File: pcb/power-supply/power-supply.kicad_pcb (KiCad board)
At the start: 2 copper layers, 2 parts

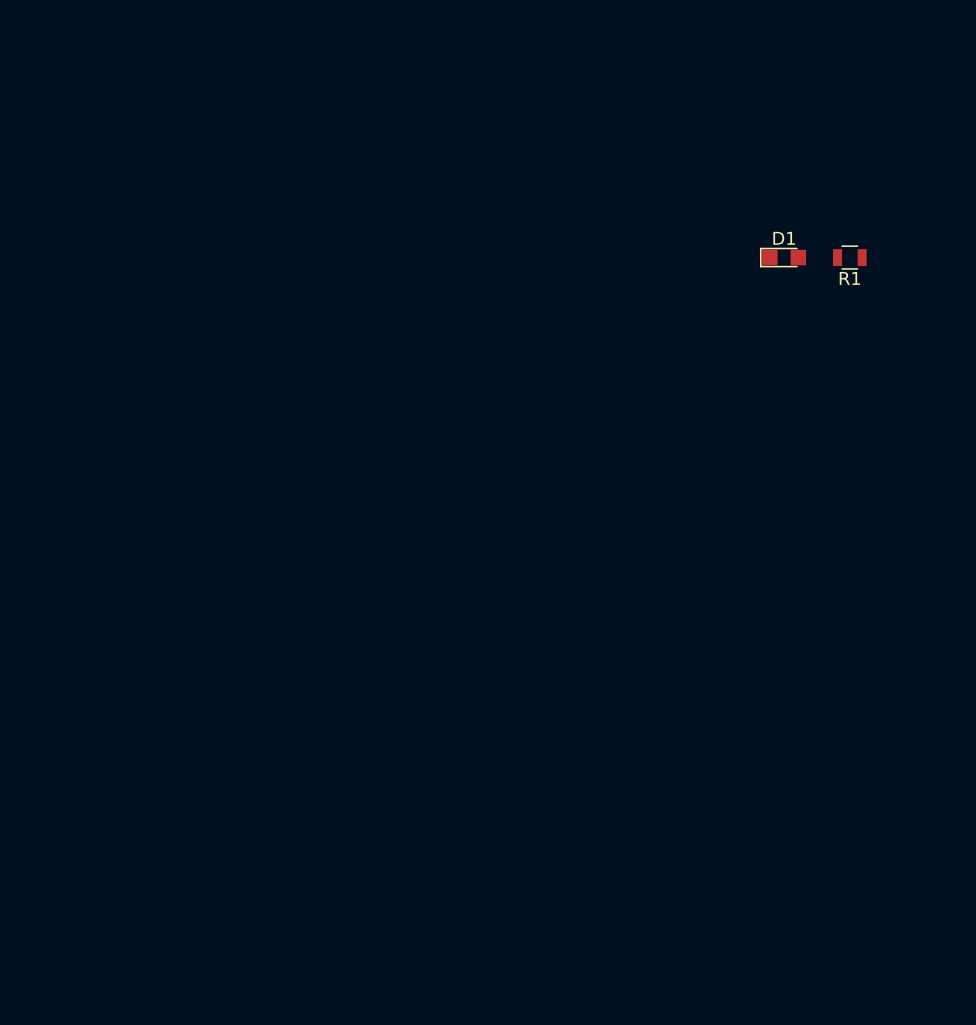
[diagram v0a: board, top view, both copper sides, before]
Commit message: starting the pcb circuit design and the layout design. implementing a RJ45 plug, spi pin-header, adc inputs etc
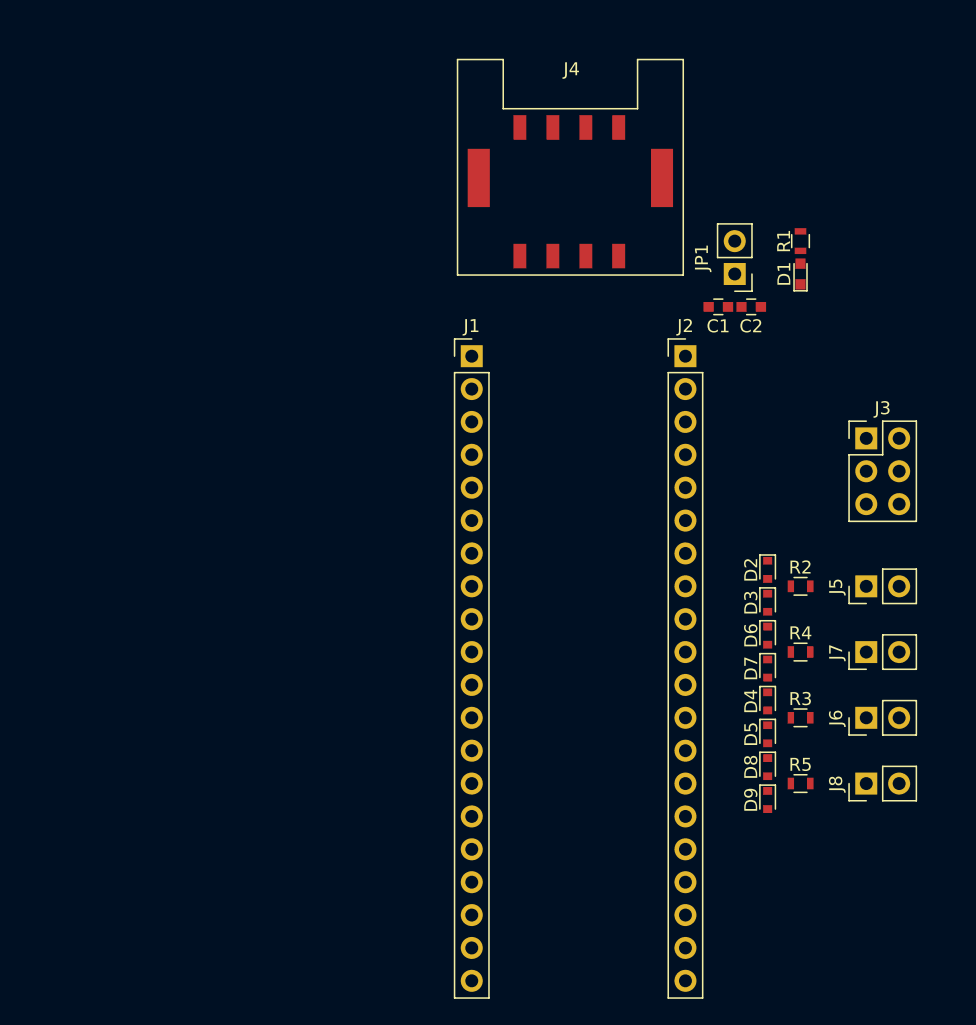
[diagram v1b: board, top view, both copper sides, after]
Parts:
- added C1: 100n, Capacitors_SMD:C_0603, F.Cu at (135.9, 113.0)
- added C2: 100n, Capacitors_SMD:C_0603, F.Cu at (138.4, 113.0)
- added D2: D, Diodes_SMD:D_SOD-523, F.Cu at (139.7, 133.3)
- added D3: D, Diodes_SMD:D_SOD-523, F.Cu at (139.7, 135.9)
- added D4: D, Diodes_SMD:D_SOD-523, F.Cu at (139.7, 143.5)
- added D5: D, Diodes_SMD:D_SOD-523, F.Cu at (139.7, 146.1)
- added D6: D, Diodes_SMD:D_SOD-523, F.Cu at (139.7, 138.4)
- added D7: D, Diodes_SMD:D_SOD-523, F.Cu at (139.7, 141.0)
- added D8: D, Diodes_SMD:D_SOD-523, F.Cu at (139.7, 148.6)
- added D9: D, Diodes_SMD:D_SOD-523, F.Cu at (139.7, 151.1)
- added J1: Conn_01x20_Female, Socket_Strips:Socket_Strip_Straight_1x20_Pitch2.54mm, F.Cu at (116.8, 116.8)
- added J2: Conn_01x20_Female, Socket_Strips:Socket_Strip_Straight_1x20_Pitch2.54mm, F.Cu at (133.3, 116.8)
- added J3: Conn_02x03, Pin_Headers:Pin_Header_Straight_2x03_Pitch2.54mm, F.Cu at (147.3, 123.2)
- added J4: RJ45, Connectors:IQRF_KON-SIM-01, F.Cu at (124.5, 104.1)
- added J5: Conn_01x02, Pin_Headers:Pin_Header_Straight_1x02_Pitch2.54mm, F.Cu at (147.3, 134.6)
- added J6: Conn_01x02, Pin_Headers:Pin_Header_Straight_1x02_Pitch2.54mm, F.Cu at (147.3, 144.8)
- added J7: Conn_01x02, Pin_Headers:Pin_Header_Straight_1x02_Pitch2.54mm, F.Cu at (147.3, 139.7)
- added J8: Conn_01x02, Pin_Headers:Pin_Header_Straight_1x02_Pitch2.54mm, F.Cu at (147.3, 149.9)
- added JP1: JP, Pin_Headers:Pin_Header_Straight_1x02_Pitch2.54mm, F.Cu at (137.2, 110.5)
- added R2: 100k, Resistors_SMD:R_0603, F.Cu at (142.2, 134.6)
- added R3: 100k, Resistors_SMD:R_0603, F.Cu at (142.2, 144.8)
- added R4: 100k, Resistors_SMD:R_0603, F.Cu at (142.2, 139.7)
- added R5: 100k, Resistors_SMD:R_0603, F.Cu at (142.2, 149.9)
- D1: footprint LEDs:LED_0805 -> LEDs:LED_0603
- R1: value R -> 150; footprint Resistors_SMD:R_0805 -> Resistors_SMD:R_0603
- moved R1 4.02 mm to (142.2, 108.0), turned to 270 degrees
- moved D1 1.80 mm to (142.2, 110.5), turned to 90 degrees
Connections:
- R1 pad 1: VCC -> +5V

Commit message: removed RJ45 (should have been a RJ11) with a simple 03x01 pinheader for uart
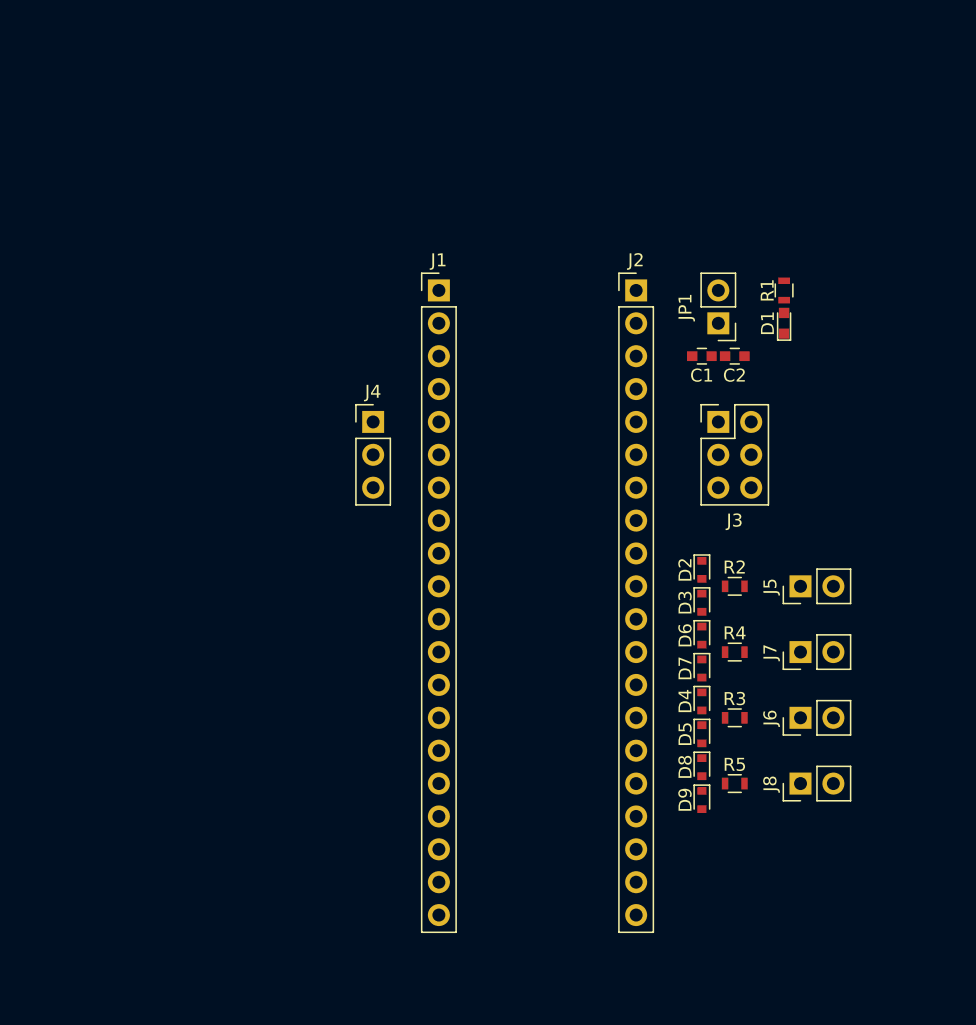
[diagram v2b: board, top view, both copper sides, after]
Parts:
- J4: value RJ45 -> Conn_01x03; footprint Connectors:IQRF_KON-SIM-01 -> Pin_Headers:Pin_Header_Straight_1x03_Pitch2.54mm
- moved J4 23.4 mm to (109.2, 121.9)
- moved J3 11.5 mm to (135.9, 121.9)
- moved J2 6.35 mm to (129.5, 111.8)
- moved J1 5.68 mm to (114.3, 111.8)
- moved R2 5.08 mm to (137.2, 134.6)
- moved R3 5.08 mm to (137.2, 144.8)
- moved R4 5.08 mm to (137.2, 139.7)
- moved R5 5.08 mm to (137.2, 149.9)
- moved D2 5.08 mm to (134.6, 133.3)
- moved D3 5.08 mm to (134.6, 135.9)
- moved D4 5.08 mm to (134.6, 143.5)
- moved D5 5.08 mm to (134.6, 146.1)
- moved D6 5.08 mm to (134.6, 138.4)
- moved D7 5.08 mm to (134.6, 141.0)
- moved D8 5.08 mm to (134.6, 148.6)
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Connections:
- J4 pad 1: Net-(J4-Pad1) -> /D2
- J4 pad 2: /D2 -> /D3
- J4 pad 3: /D3 -> GND

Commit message: added the teensy schematic and footprint lib to the project, added the project from mr veigl to git, added teensy++2.0 to the schematic, added molex connectors, 02x05 pinheaders for motor control signals
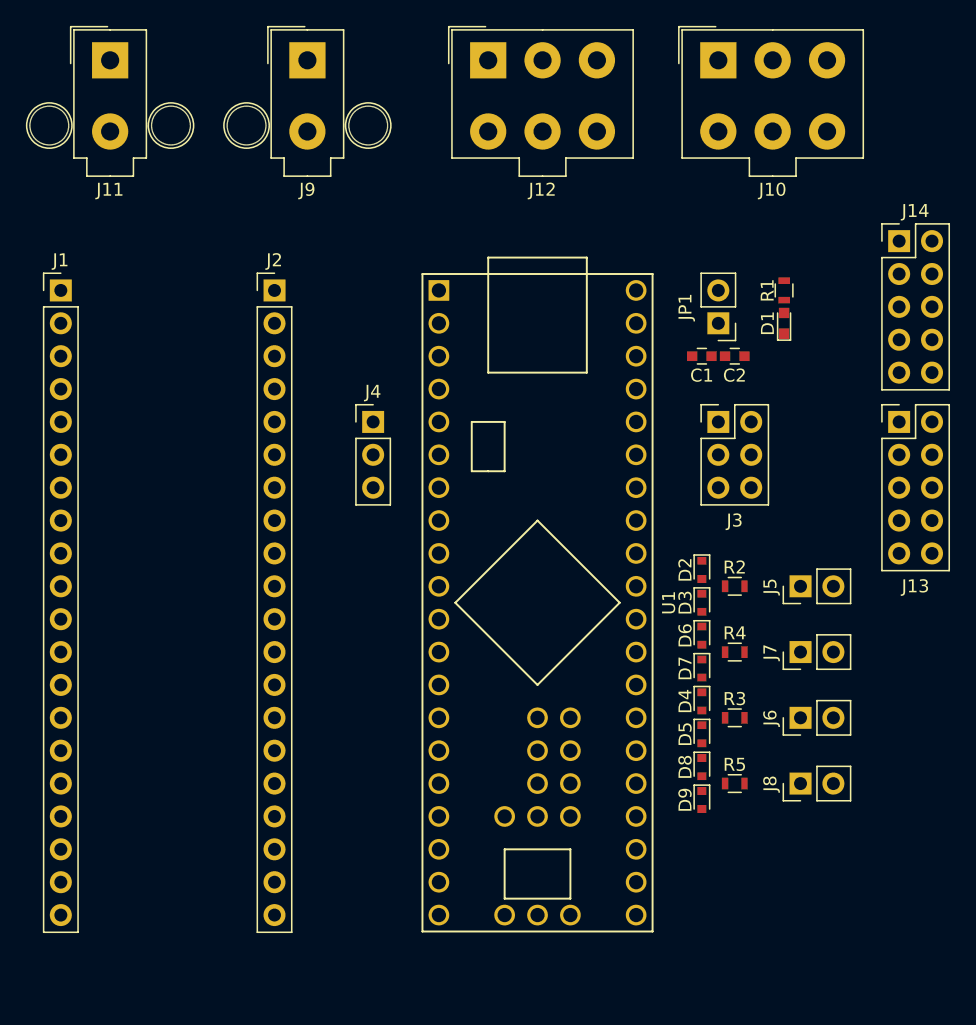
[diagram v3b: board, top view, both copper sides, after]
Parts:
- added J10: Pwr_Terminal, Connectors_Molex:Molex_MiniFit-JR-5556-06A_2x03x4.20mm_Straight, F.Cu at (135.9, 94.0)
- added J11: Pwr_Terminal, Connectors_Molex:Molex_MiniFit-JR-5556-02B_2x01x4.20mm_Straight, F.Cu at (88.9, 94.0)
- added J12: Pwr_Terminal, Connectors_Molex:Molex_MiniFit-JR-5556-06A_2x03x4.20mm_Straight, F.Cu at (118.1, 94.0)
- added J13: Conn_02x05, Pin_Headers:Pin_Header_Straight_2x05_Pitch2.54mm, F.Cu at (149.9, 121.9)
- added J14: Conn_02x05, Pin_Headers:Pin_Header_Straight_2x05_Pitch2.54mm, F.Cu at (149.9, 108.0)
- added J9: Pwr_Terminal, Connectors_Molex:Molex_MiniFit-JR-5556-02B_2x01x4.20mm_Straight, F.Cu at (104.1, 94.0)
- added U1: Teensy++2.0, Teensy:Teensy2.0++, F.Cu at (121.9, 135.9)
- moved J1 29.2 mm to (85.1, 111.8)
- moved J2 27.9 mm to (101.6, 111.8)
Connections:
- net /B4 renamed Net-(J2-Pad4)
- net /B5 renamed Net-(J2-Pad3)
- net /B6 renamed Net-(J2-Pad2)
- net /B7 renamed Net-(J1-Pad2)
- net /C0 renamed Net-(J1-Pad13)
- net /C1 renamed Net-(J1-Pad14)
- net /C2 renamed Net-(J1-Pad15)
- net /C3 renamed Net-(J1-Pad16)
- net /C4 renamed Net-(J1-Pad17)
- net /C5 renamed Net-(J1-Pad18)
- net /C6 renamed Net-(J1-Pad19)
- net /C7 renamed Net-(J1-Pad20)
- net /D0 renamed Net-(J1-Pad3)
- net /D1 renamed Net-(J1-Pad4)
- net /D4 renamed Net-(J1-Pad7)
- net /D5 renamed Net-(J1-Pad8)
- net /D6 renamed Net-(J1-Pad9)
- net /D7 renamed Net-(J1-Pad10)
- net /E0 renamed Net-(J1-Pad11)
- net /E1 renamed Net-(J1-Pad12)
- net /E6 renamed Net-(J2-Pad10)
- net /E7 renamed Net-(J2-Pad9)
- net /F4 renamed Net-(J2-Pad17)
- net /F5 renamed Net-(J2-Pad18)
- net /F6 renamed Net-(J2-Pad19)
- net /F7 renamed Net-(J2-Pad20)
- net /VREF renamed Net-(J2-Pad12)
- J1 pad 1: GND -> Net-(J1-Pad1)
- J1 pad 5: /D2 -> Net-(J1-Pad5)
- J1 pad 6: /D3 -> Net-(J1-Pad6)
- J2 pad 1: Net-(C1-Pad1) -> Net-(J2-Pad1)
- J2 pad 11: GND -> Net-(J2-Pad11)
- J2 pad 13: /F0 -> Net-(J2-Pad13)
- J2 pad 14: /F1 -> Net-(J2-Pad14)
- J2 pad 15: /F2 -> Net-(J2-Pad15)
- J2 pad 16: /F3 -> Net-(J2-Pad16)
- J2 pad 5: /B3 -> Net-(J2-Pad5)
- J2 pad 6: /B2 -> Net-(J2-Pad6)
- J2 pad 7: /B1 -> Net-(J2-Pad7)
- J2 pad 8: /B0 -> Net-(J2-Pad8)
